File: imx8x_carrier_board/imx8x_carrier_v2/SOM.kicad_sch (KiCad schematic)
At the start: 41 parts, among them J1 BTH-070-02-L-D-A, J4 BTH-070-02-L-D-A

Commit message: Changes some things
Made them all DF11. We have tons. And they can be secure.
Updated PinMux Sheet. 1 of everything, while also using whats preconfigured on the dev board for some stuff. Its good for final review before ordering. This should work.
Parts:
- H1, H2, H3, H4: footprint MountingHole:MountingHole_3.2mm_M3_ISO7380_Pad -> MountingHole:MountingHole_2.7mm_M2.5_DIN965_Pad
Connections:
- net X_ADMA_I2C0_SCL: now reaches J4.66 (D33)
- net X_ADMA_I2C0_SDA: now reaches J4.68 (D34)
- no-connect marks 86 -> 84
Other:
- moved on the sheet: TP2
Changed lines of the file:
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@@
 		)
 	)
-	(text_box "I2C0_SCL/SDA is where the INA260s will communicate over. Their addresses are set on the EPS_REVE Schematic."
+	(text_box "In the kernel device tree you can set the correct value to the specific register and enable, disable, or leave floating the pull up or down of the pin, controlled on the actual SOM\n"
 		(exclude_from_sim no)
-		(at 268.097 126.746 0)
+		(at 12.7 111.125 0)
+		(size 36.195 37.465)
+		(margins 0.9525 0.9525 0.9525 0.9525)
+		(stroke
+			(width 0)
+			(type solid)
+		)
+		(fill
+			(type none)
+		)
+		(effects
+			(font
+				(size 1.27 1.27)
+			)
+			(justify left top)
+		)
+	)
+	(text_box "I2C0_SCL/SDA Reserved for Power Board Diagnostics. \nI2C3_SCL/SDA is open for end user."
+		(exclude_from_sim no)
+		(at 264.16 136.525 0)
 		(size 38.1 10.16)
 		(margins 0.9525 0.9525 0.9525 0.9525)
@@
 	)
 	(junction
+		(at 218.44 177.8)
+		(diameter 0)
+		(color 0 0 0 0)
+	)
+	(junction
 		(at 219.71 223.52)
 		(diameter 0)
@@
 	)
 	(no_connect
-		(at 246.38 129.54)
-	)
-	(no_connect
 		(at 76.2 179.07)
 	)
@@
 	)
 	(no_connect
-		(at 246.38 132.08)
-	)
-	(no_connect
 		(at 76.2 143.51)
 	)
@@
 	(wire
 		(pts
+			(xy 246.38 129.54) (xy 251.46 129.54)
+		)
+		(stroke
+			(width 0)
+			(type default)
+		)
+	)
+	(wire
+		(pts
 			(xy 220.98 132.08) (xy 215.9 132.08)
 		)
@@
 	(wire
 		(pts
+			(xy 218.44 177.8) (xy 220.98 177.8)
+		)
+		(stroke
+			(width 0)
+			(type default)
+		)
+	)
+	(wire
+		(pts
 			(xy 101.6 212.09) (xy 106.68 212.09)
 		)
@@
 	(wire
 		(pts
-			(xy 102.87 204.47) (xy 102.87 222.25)
+			(xy 262.89 127) (xy 274.32 127)
 		)
 		(stroke
@@
 	(wire
 		(pts
-			(xy 74.93 158.75) (xy 74.93 176.53)
+			(xy 102.87 204.47) (xy 102.87 222.25)
 		)
 		(stroke
@@
 	(wire
 		(pts
-			(xy 251.46 152.4) (xy 251.46 154.94)
+			(xy 74.93 158.75) (xy 74.93 176.53)
 		)
 		(stroke
@@
 	(wire
 		(pts
-			(xy 168.91 210.82) (xy 220.98 210.82)
+			(xy 246.38 132.08) (xy 251.46 132.08)
 		)
 		(stroke
@@
 	(wire
 		(pts
-			(xy 74.93 123.19) (xy 74.93 107.95)
+			(xy 251.46 152.4) (xy 251.46 154.94)
 		)
 		(stroke
@@
 	(wire
 		(pts
-			(xy 223.52 240.03) (xy 229.87 240.03)
+			(xy 168.91 210.82) (xy 220.98 210.82)
 		)
 		(stroke
@@
 	(wire
 		(pts
-			(xy 219.71 182.88) (xy 219.71 167.64)
+			(xy 74.93 123.19) (xy 74.93 107.95)
 		)
 		(stroke
@@
 	(wire
 		(pts
-			(xy 246.38 190.5) (xy 280.67 190.5)
+			(xy 223.52 240.03) (xy 229.87 240.03)
 		)
 		(stroke
@@
 	(wire
 		(pts
-			(xy 215.9 114.3) (xy 215.9 111.76)
+			(xy 246.38 190.5) (xy 280.67 190.5)
 		)
 		(stroke
@@
 	(wire
 		(pts
-			(xy 102.87 158.75) (xy 102.87 171.45)
+			(xy 215.9 114.3) (xy 215.9 111.76)
 		)
 		(stroke
@@
 	(wire
 		(pts
-			(xy 248.92 172.72) (xy 246.38 172.72)
+			(xy 102.87 158.75) (xy 102.87 171.45)
 		)
 		(stroke
@@
 	(wire
 		(pts
-			(xy 215.9 88.9) (xy 215.9 91.44)
+			(xy 248.92 172.72) (xy 246.38 172.72)
 		)
 		(stroke
@@
 	(wire
 		(pts
-			(xy 264.16 127) (xy 262.89 127)
+			(xy 215.9 88.9) (xy 215.9 91.44)
 		)
 		(stroke
@@
 	(wire
 		(pts
+			(xy 219.71 182.88) (xy 219.71 193.04)
+		)
+		(stroke
+			(width 0)
+			(type default)
+		)
+	)
+	(wire
+		(pts
 			(xy 246.38 215.9) (xy 247.65 215.9)
 		)
@@
 	(wire
 		(pts
+			(xy 215.9 177.8) (xy 218.44 177.8)
+		)
+		(stroke
+			(width 0)
+			(type default)
+		)
+	)
+	(wire
+		(pts
 			(xy 101.6 156.21) (xy 106.68 156.21)
 		)
@@
 	(wire
 		(pts
+			(xy 219.71 167.64) (xy 219.71 182.88)
+		)
+		(stroke
+			(width 0)
+			(type default)
+		)
+	)
+	(wire
+		(pts
 			(xy 246.38 213.36) (xy 247.65 213.36)
 		)
@@
 	(wire
 		(pts
-			(xy 264.16 129.54) (xy 264.16 127)
+			(xy 274.32 129.54) (xy 274.32 127)
 		)
 		(stroke
@@
 	(wire
 		(pts
-			(xy 203.2 177.8) (xy 220.98 177.8)
-		)
-		(stroke
-			(width 0)
-			(type default)
-		)
-	)
-	(wire
-		(pts
 			(xy 88.9 227.33) (xy 74.93 227.33)
 		)
@@
 	(wire
 		(pts
-			(xy 219.71 193.04) (xy 219.71 182.88)
-		)
-		(stroke
-			(width 0)
-			(type default)
-		)
-	)
-	(wire
-		(pts
 			(xy 101.6 204.47) (xy 102.87 204.47)
 		)
@@
 		)
 	)
+	(global_label "X_ADMA_I2C0_SCL"
+		(shape output)
+		(at 251.46 129.54 0)
+		(fields_autoplaced yes)
+		(effects
+			(font
+				(size 1.27 1.27)
+			)
+			(justify left)
+		)
+		(property "Intersheetrefs" "${INTERSHEET_REFS}"
+			(at 271.2575 129.54 0)
+			(effects
+				(font
+					(size 1.27 1.27)
+				)
+				(justify left)
+				(hide yes)
+			)
+		)
+	)
 	(global_label "~{X_nRESET_IN}"
 		(shape input)
@@
 		)
 	)
+	(global_label "X_ADMA_I2C0_SDA"
+		(shape bidirectional)
+		(at 251.46 132.08 0)
+		(fields_autoplaced yes)
+		(effects
+			(font
+				(size 1.27 1.27)
+			)
+			(justify left)
+		)
+		(property "Intersheetrefs" "${INTERSHEET_REFS}"
+			(at 272.4293 132.08 0)
+			(effects
+				(font
+					(size 1.27 1.27)
+				)
+				(justify left)
+				(hide yes)
+			)
+		)
+	)
 	(global_label "X_POR_B_3V3"
 		(shape input)
-		(at 203.2 177.8 180)
+		(at 215.9 177.8 180)
 		(fields_autoplaced yes)
 		(effects
@@
 		)
 		(property "Intersheetrefs" "${INTERSHEET_REFS}"
-			(at 187.4544 177.8 0)
+			(at 200.1544 177.8 0)
 			(effects
 				(font
@@
 	)
 	(global_label "X_ADMA_I2C3_SCL"
-		(shape input)
+		(shape output)
 		(at 106.68 186.69 0)
 		(fields_autoplaced yes)
@@
 			)
 		)
-		(property "Footprint" "MountingHole:MountingHole_3.2mm_M3_ISO7380_Pad"
+		(property "Footprint" "MountingHole:MountingHole_2.7mm_M2.5_DIN965_Pad"
 			(at 373.38 29.21 0)
 			(effects
@@
 			)
 		)
-		(property "Footprint" "MountingHole:MountingHole_3.2mm_M3_ISO7380_Pad"
+		(property "Footprint" "MountingHole:MountingHole_2.7mm_M2.5_DIN965_Pad"
 			(at 355.6 29.21 0)
 			(effects
@@
 			)
 		)
-		(property "Footprint" "MountingHole:MountingHole_3.2mm_M3_ISO7380_Pad"
+		(property "Footprint" "MountingHole:MountingHole_2.7mm_M2.5_DIN965_Pad"
 			(at 382.27 29.21 0)
 			(effects
@@
 	(symbol
 		(lib_id "power:GND")
-		(at 264.16 129.54 0)
+		(at 274.32 129.54 0)
 		(unit 1)
 		(exclude_from_sim no)
@@
 		(fields_autoplaced yes)
 		(property "Reference" "#PWR0151"
-			(at 264.16 135.89 0)
+			(at 274.32 135.89 0)
 			(effects
 				(font
@@
 		)
 		(property "Value" "GND"
-			(at 264.16 134.62 0)
+			(at 274.32 134.62 0)
 			(effects
 				(font
@@
 		)
 		(property "Footprint" ""
-			(at 264.16 129.54 0)
+			(at 274.32 129.54 0)
 			(effects
 				(font
@@
 		)
 		(property "Datasheet" ""
-			(at 264.16 129.54 0)
+			(at 274.32 129.54 0)
 			(effects
 				(font
@@
 		)
 		(property "Description" "Power symbol creates a global label with name \"GND\" , ground"
-			(at 264.16 129.54 0)
+			(at 274.32 129.54 0)
 			(effects
 				(font
@@
 			)
 		)
-		(property "Footprint" "MountingHole:MountingHole_3.2mm_M3_ISO7380_Pad"
+		(property "Footprint" "MountingHole:MountingHole_2.7mm_M2.5_DIN965_Pad"
 			(at 364.49 29.21 0)
 			(effects
@@
 	(symbol
 		(lib_id "Connector:TestPoint")
-		(at 203.2 177.8 180)
+		(at 218.44 177.8 180)
 		(unit 1)
 		(exclude_from_sim no)
@@
 		(dnp no)
 		(property "Reference" "TP2"
-			(at 202.184 181.102 0)
+			(at 221.996 176.784 0)
 			(effects
 				(font
@@
 		)
 		(property "Value" "TestPoint"
-			(at 202.946 178.816 0)
+			(at 218.186 178.816 0)
 			(effects
 				(font
@@
 		)
 		(property "Footprint" "TestPoint:TestPoint_THTPad_1.0x1.0mm_Drill0.5mm"
-			(at 198.12 177.8 0)
+			(at 213.36 177.8 0)
 			(effects
 				(font
@@
 		)
 		(property "Datasheet" "~"
-			(at 198.12 177.8 0)
+			(at 213.36 177.8 0)
 			(effects
 				(font
@@
 		)
 		(property "Description" "test point"
-			(at 203.2 177.8 0)
+			(at 218.44 177.8 0)
 			(effects
 				(font
@@
 		)
 		(property "LCSC" ""
-			(at 203.2 177.8 0)
+			(at 218.44 177.8 0)
 			(effects
 				(font
@@
 		)
 		(property "Voltage" ""
-			(at 203.2 177.8 0)
+			(at 218.44 177.8 0)
 			(effects
 				(font
@@
 		(dnp no)
 		(property "Reference" "R126"
-			(at 263.525 125.73 90)
+			(at 273.685 125.73 90)
 			(effects
 				(font

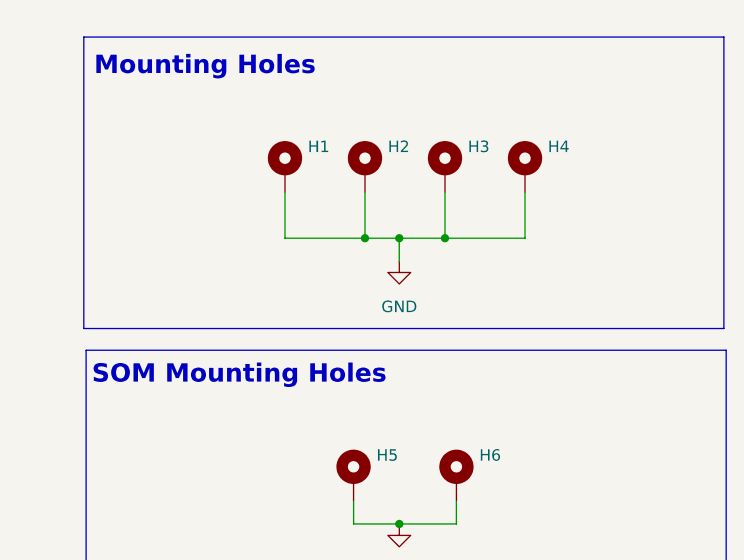
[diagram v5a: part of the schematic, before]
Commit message: Final Gerbers, Fixed mounting holes
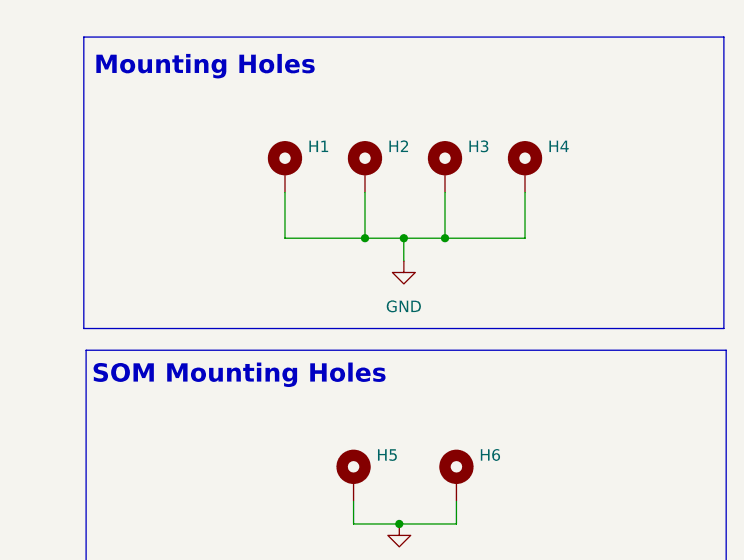
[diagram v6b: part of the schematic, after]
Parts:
- H1, H2, H3, H4: value M3 -> MountingHole_Pad_M2.5_2.7mm; footprint MountingHole:MountingHole_2.7mm_M2.5_DIN965_Pad -> MountingHole:MountingHole_3.2mm_M3_DIN965_Pad
